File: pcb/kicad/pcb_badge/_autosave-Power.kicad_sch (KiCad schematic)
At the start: 36 parts, among them J1 USB_C_Receptacle_USB2.0_16P, J2 Conn_01x02_Pin, J6 USB_SMT, Q1 SI2302, Q9 JSM2301S, U1 TLV70328DBVR, U2 QX2304L33F

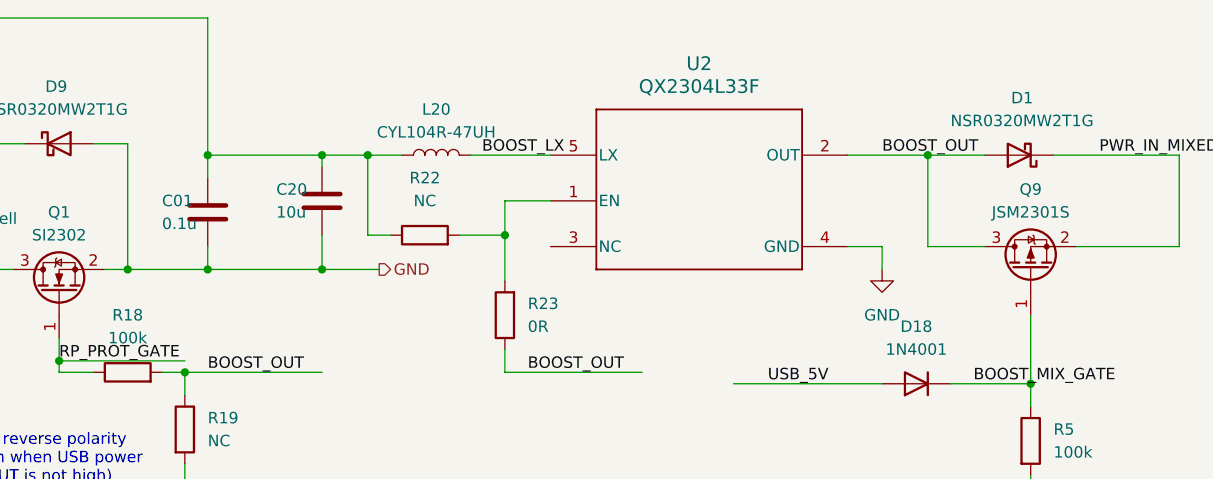
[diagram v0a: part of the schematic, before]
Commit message: Correct FET footprint
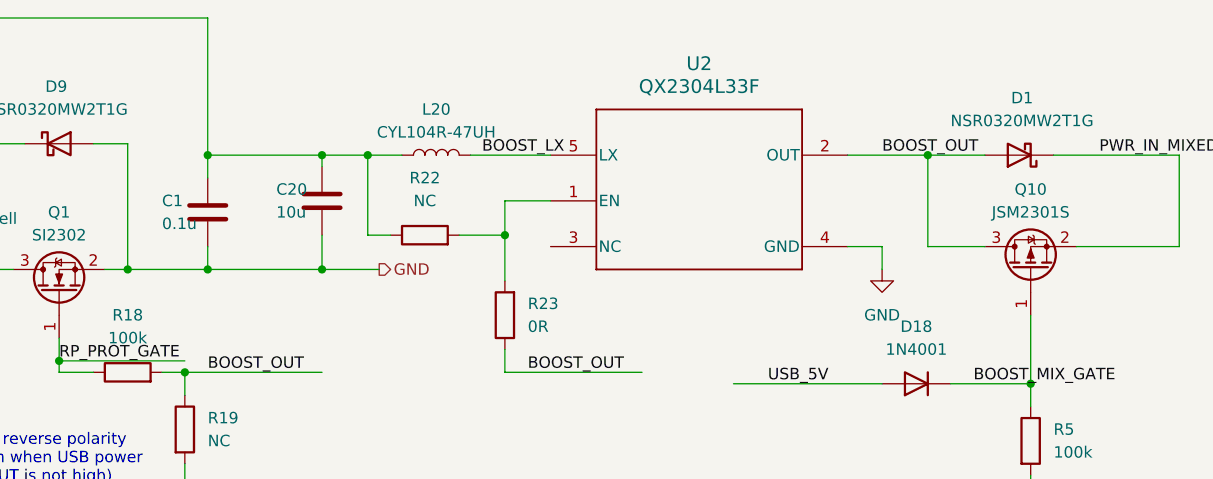
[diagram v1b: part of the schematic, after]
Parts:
- renumbered C01 to C1, Q9 to Q10
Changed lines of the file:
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@@
 		(on_board yes)
 		(dnp no)
-		(property "Reference" "C01"
+		(property "Reference" "C1"
 			(at 87.63 39.37 0)
 			(effects
@@
 			(project "pcb_badge"
 				(path "/5e1f2779-68ae-4a90-b87f-237568be093e/5b14d099-1603-44e2-9137-5cf230eeec9a"
-					(reference "C01")
+					(reference "C1")
 					(unit 1)
 				)
@@
 		(dnp no)
 		(fields_autoplaced yes)
-		(property "Reference" "Q9"
+		(property "Reference" "Q10"
 			(at 184.15 38.1 90)
 			(effects
@@
 			(project "pcb_badge"
 				(path "/5e1f2779-68ae-4a90-b87f-237568be093e/5b14d099-1603-44e2-9137-5cf230eeec9a"
-					(reference "Q9")
-					(unit 1)
-				)
+					(reference "Q10")
+					(unit 1)
+				)
